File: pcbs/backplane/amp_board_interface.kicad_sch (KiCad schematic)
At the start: 20 parts

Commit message: Schematic file fix, misc. PCB
Fixed issue with KiCAD's automatic V5→V6 migration (corrected in 6.0.11) that caused problems with component references in multi-channel schematic sheets
Finished migration in amp ctrl PCB, inc. re-assigning "exclude from BOM" attributes to testpoints, solder jumpers
Added mounting hole to amp ctrl PCB for addl support to Ethernet jacks, power connector through stiffener
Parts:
- C? (x2): renamed from ?; value 100nF 50V X7R -> (none); footprint Capacitor_SMD:C_0603_1608Metric -> (none)
- C?: renamed from ?; value 1uF 50V X7R -> (none); footprint Capacitor_SMD:C_0805_2012Metric -> (none)
- D?: renamed from ?; value Red -> (none); footprint LED_SMD:LED_0805_2012Metric -> (none)
- J4, J6, J7: renamed from ?; value RJ45_Shielded -> (none); footprint Martinos:RJ45_Amphenol_RJE06-188-1x20 -> (none)
- Q1: renamed from ?; value MMBT3904 -> (none); footprint Package_TO_SOT_SMD:SOT-23 -> (none)
- R?: renamed from ?; value 3.3K -> (none); footprint Resistor_SMD:R_0805_2012Metric -> (none)
- R? (x2): renamed from ?; value 1K -> (none); footprint Resistor_SMD:R_0805_2012Metric -> (none)
- R? (x2): renamed from ?; value 20K -> (none); footprint Resistor_SMD:R_0805_2012Metric -> (none)
- TP19: renamed from ?; value TestPoint_Flag -> (none); footprint TestPoint:TestPoint_Keystone_5019_Minature -> (none)
- TP21, TP26, TP54: renamed from ?; value TestPoint -> (none); footprint TestPoint:TestPoint_Pad_D2.0mm -> (none)
- U1: renamed from ?; value 74LVC1G14 -> (none); footprint Martinos_std:SOT-23-5 -> (none)
- U16: renamed from ?; value 74LVC2G02 -> (none); footprint Package_SO:VSSOP-8_3.0x3.0mm_P0.65mm -> (none)

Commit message: Amp ctrl: lengthened ADC & DAC reset delay to ~50 ms (#14) Backplane: added clock multiplier for 10 Mhz scanner clock (fixes #21) Backplane: reduced R5 from 10 to 1 ohm, to avoid excessive voltage drop (#20) Backplane: replaced 15V regulator with efficient voltage limiter (#20) Backplane: changed all mounting holes to signal ground Backplane: replaced +2.5V regulator with a higher-current model to support FPGA I/O bank current draw Updated to KiCAD 8
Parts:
- C1, C38: renamed from C?; value (none) -> 100nF 50V X7R; footprint (none) -> Capacitor_SMD:C_0603_1608Metric
- C39: renamed from C?; value (none) -> 1uF 50V X7R; footprint (none) -> Capacitor_SMD:C_0805_2012Metric
- D4: renamed from D?; value (none) -> Red; footprint (none) -> LED_SMD:LED_0805_2012Metric
- J4, J6, J7: value (none) -> RJ45_Shielded; footprint (none) -> Martinos:RJ45_Amphenol_RJE06-188-1x20
- Q1: value (none) -> MMBT3904; footprint (none) -> Package_TO_SOT_SMD:SOT-23
- R16, R66: renamed from R?; value (none) -> 1K; footprint (none) -> Resistor_SMD:R_0805_2012Metric
- R17: renamed from R?; value (none) -> 3.3K; footprint (none) -> Resistor_SMD:R_0805_2012Metric
- R63, R64: renamed from R?; value (none) -> 20K; footprint (none) -> Resistor_SMD:R_0805_2012Metric
- TP19: value (none) -> TestPoint_Flag; footprint (none) -> TestPoint:TestPoint_Keystone_5019_Minature
- TP21, TP26, TP54: value (none) -> TestPoint; footprint (none) -> TestPoint:TestPoint_Pad_D2.0mm
- U1: value (none) -> 74LVC1G14; footprint (none) -> Martinos_std:SOT-23-5
- U16: value (none) -> 74LVC2G02; footprint (none) -> Package_SO:VSSOP-8_3.0x3.0mm_P0.65mm

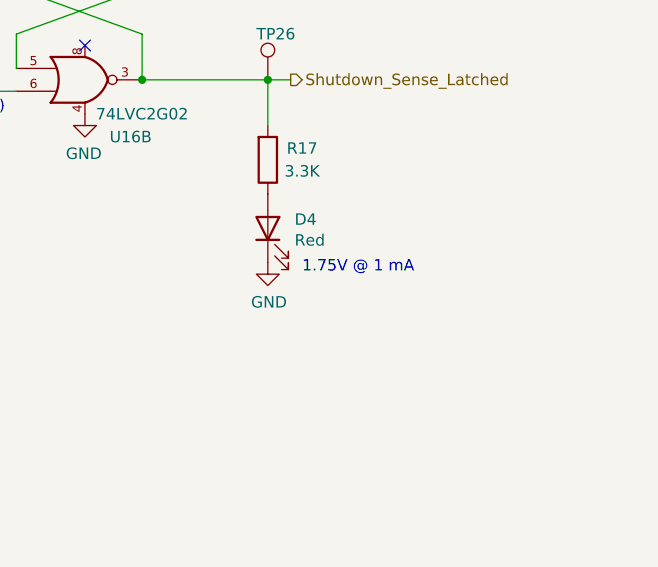
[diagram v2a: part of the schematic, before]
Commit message: Comms fix, misc. improvements
Added 33KΩ pull-ups & pull-downs to amp ctrl board's LVDS inputs, to solve issues caused by unconfigured FPGA pins during boot (fixes #23)
Swapped backplane power input polarity for consistency with power connectors (fixes #20)
Added "manual enable" optical input to backplane, for safety: requires positive enable to keep amplifiers enabled
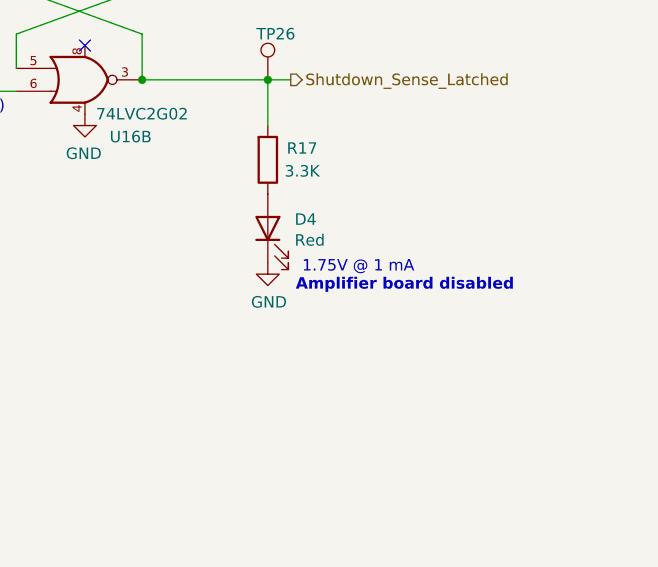
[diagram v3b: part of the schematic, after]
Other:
- note added: "Amplifier board disabled"
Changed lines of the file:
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@@
+		)
+	)
+	(text "Amplifier board disabled"
+		(exclude_from_sim no)
+		(at 228.6 74.93 0)
+		(effects
+			(font
+				(size 1.27 1.27)
+				(thickness 0.254)
+				(bold yes)
+			)
 		)
 	)

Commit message: Corrected power-up behavior
Backplane: Inverted polarity of Shutdown_Force (now Power_Enable_FPGA), to keep amps powered off until software starts: fixes #23
Backplane: Routed Shutdown_Force to unused pin 3 on RJ45 jack B to amp boards: fixes #23
Backplane: Added pull-up and pull-down resistors to fanout buffer inputs, to keep SCK & ~LDAC signals in proper state during power-on: fixes #23
Amp control: Added transistor to reset DAC & ADC from pin 3 of RJ45 jack B
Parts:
- J4, J6, J7: footprint Martinos:RJ45_Amphenol_RJE06-188-1x20 -> Don:RJ45_Amphenol_RJE06-188-1x20
- U1: footprint Martinos_std:SOT-23-5 -> Don_std:SOT-23-5
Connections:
- net Shutdown_Force: now also J6.3
- no-connect marks 4 -> 3
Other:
- moved on the sheet: J4

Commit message: Misc. cleanup for mfg & improvements
Minor backplane pinout doc corrections (SCKO5 polarity, clarified some descriptions)
Backplane: Added differential- and common-mode (to standoffs) power filtering, for EMI escaping over power wiring
Amp ctrl: Changed DAC testpoints from individual pads to Keystone 5019 for easier probing
Corrected part numbers, DNP vs. non-BOM-item indications, other misc. BOM issues
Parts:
- TP21, TP26, TP54: now left out of the parts list
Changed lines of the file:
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@@
 		(unit 1)
 		(exclude_from_sim no)
-		(in_bom yes)
+		(in_bom no)
 		(on_board yes)
 		(dnp no)
@@
 		(unit 1)
 		(exclude_from_sim no)
-		(in_bom yes)
+		(in_bom no)
 		(on_board yes)
 		(dnp no)
@@
 		(unit 1)
 		(exclude_from_sim no)
-		(in_bom yes)
+		(in_bom no)
 		(on_board yes)
 		(dnp no)

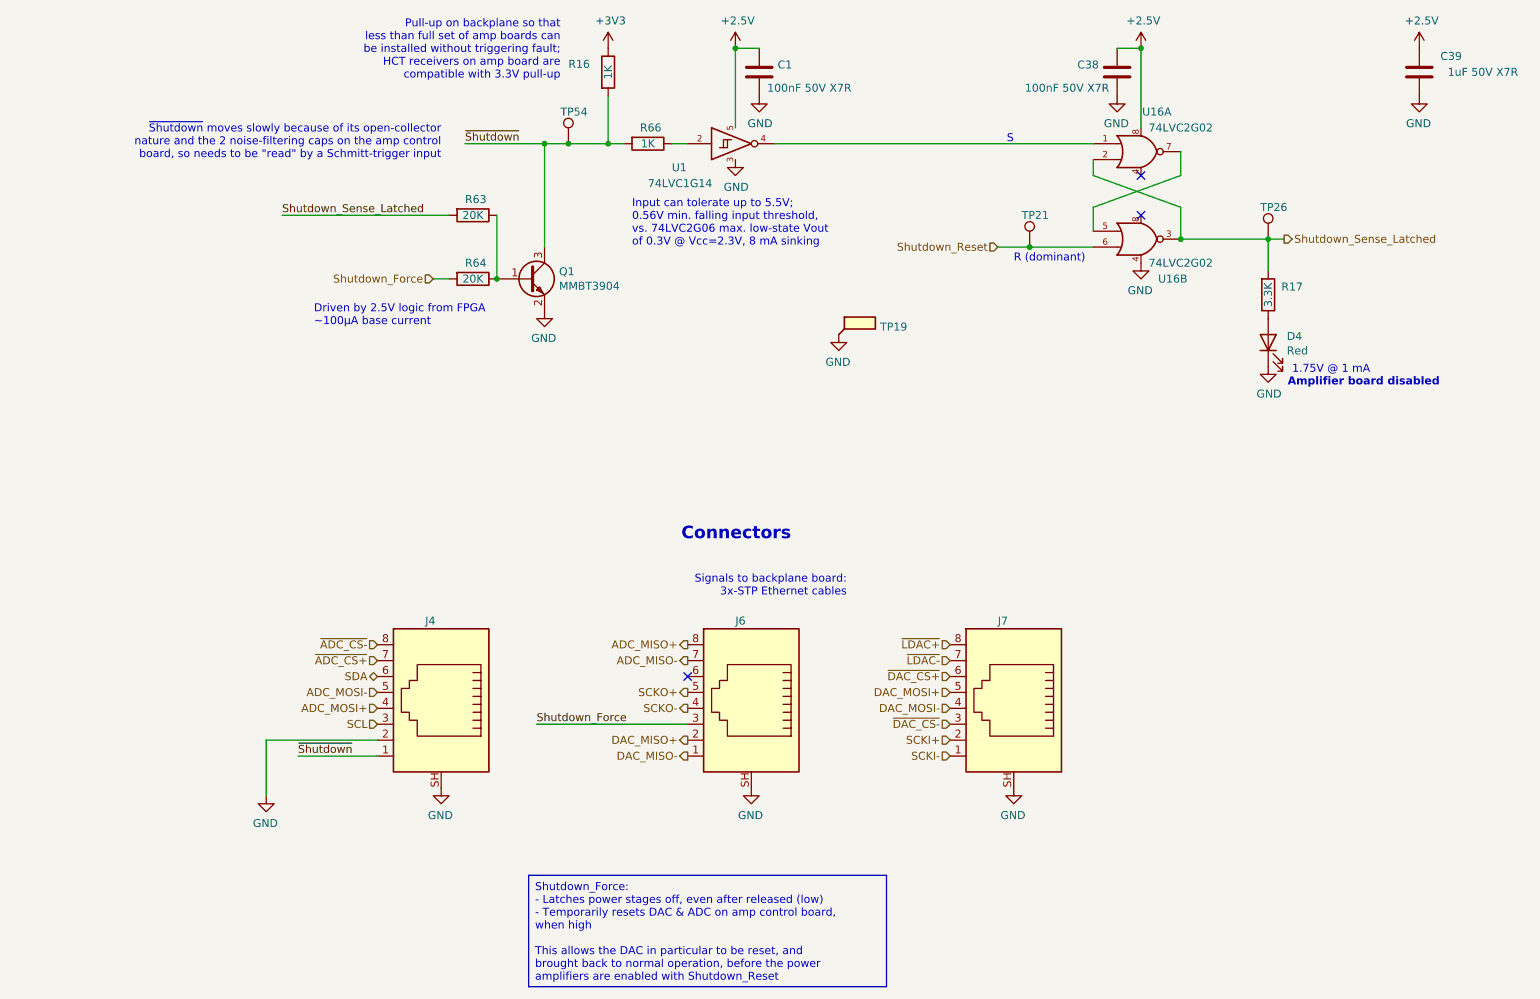
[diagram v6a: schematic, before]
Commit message: Updated KiCAD file versions to 9.0
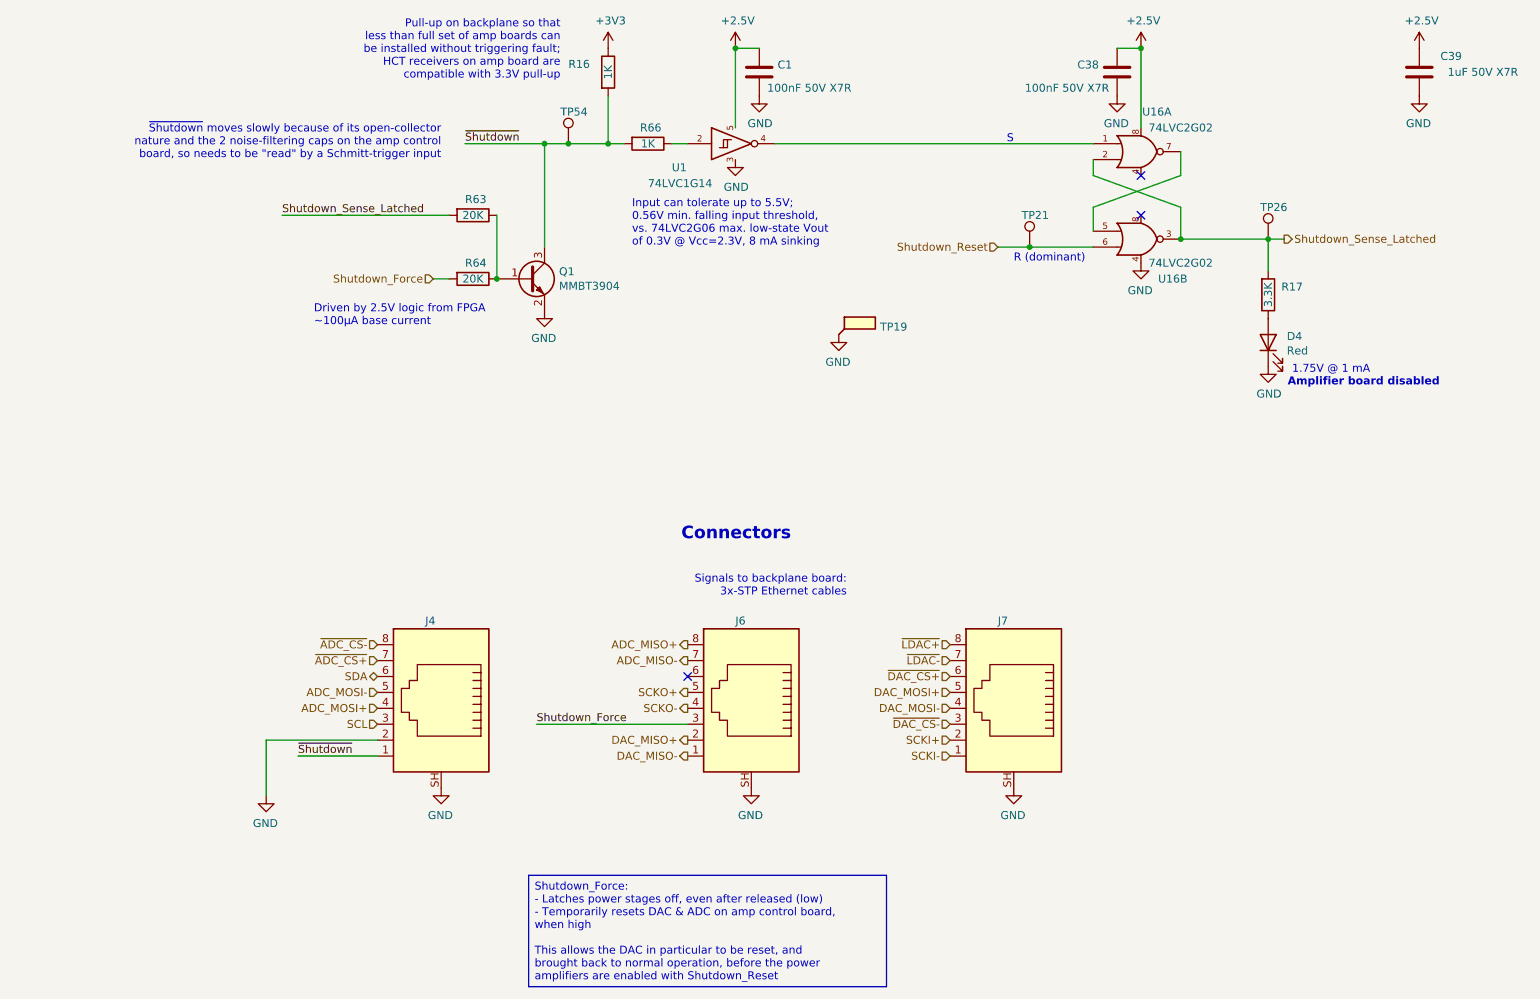
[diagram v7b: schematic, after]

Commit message: Moved all project-specific symbols & footprints into new "shim" libraries Updated projects to reference the new "shim" library
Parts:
- J4, J6, J7: footprint Don:RJ45_Amphenol_RJE06-188-1x20 -> shim:RJ45_Amphenol_RJE06-188-1x20
- U1: footprint Don_std:SOT-23-5 -> Package_TO_SOT_SMD:SOT-23-5
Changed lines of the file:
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@@
 			)
 		)
-		(property "Footprint" "Don:RJ45_Amphenol_RJE06-188-1x20"
+		(property "Footprint" "shim:RJ45_Amphenol_RJE06-188-1x20"
 			(at 130.81 126.365 90)
 			(effects
@@
 			)
 		)
-		(property "Footprint" "Don:RJ45_Amphenol_RJE06-188-1x20"
+		(property "Footprint" "shim:RJ45_Amphenol_RJE06-188-1x20"
 			(at 172.72 126.365 90)
 			(effects
@@
 			)
 		)
-		(property "Footprint" "Don:RJ45_Amphenol_RJE06-188-1x20"
+		(property "Footprint" "shim:RJ45_Amphenol_RJE06-188-1x20"
 			(at 81.28 126.365 90)
 			(effects
@@
 			)
 		)
-		(property "Footprint" "Don_std:SOT-23-5"
+		(property "Footprint" "Package_TO_SOT_SMD:SOT-23-5"
 			(at 128.27 36.83 0)
 			(effects
